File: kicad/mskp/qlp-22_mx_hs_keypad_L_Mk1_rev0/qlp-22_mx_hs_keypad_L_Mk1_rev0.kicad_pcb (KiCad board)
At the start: 2 copper layers, 23 parts, among them J1 Conn_01x12_Socket, SW0 Switch, SW1 Switch, SW10 Switch, SW2 Switch, SW3 Switch, SW4 Switch, SW5 Switch, SW6 Switch, SW7 Switch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

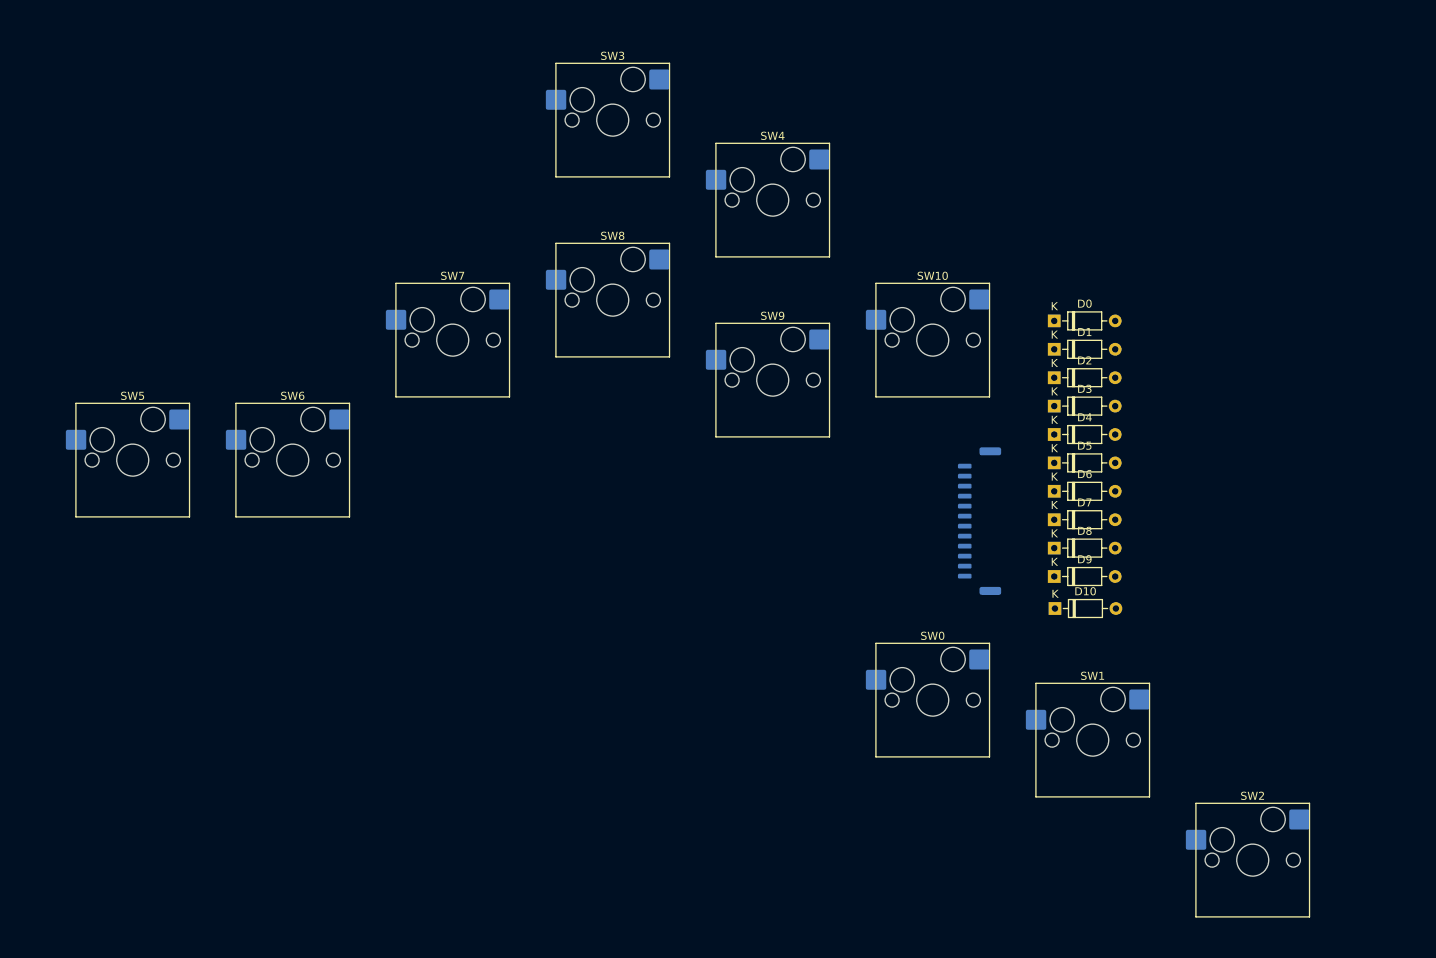
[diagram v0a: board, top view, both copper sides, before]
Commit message: Adds basic layout and edges for qlp-22_mx_hs_keypad_L_Mk1_rev0
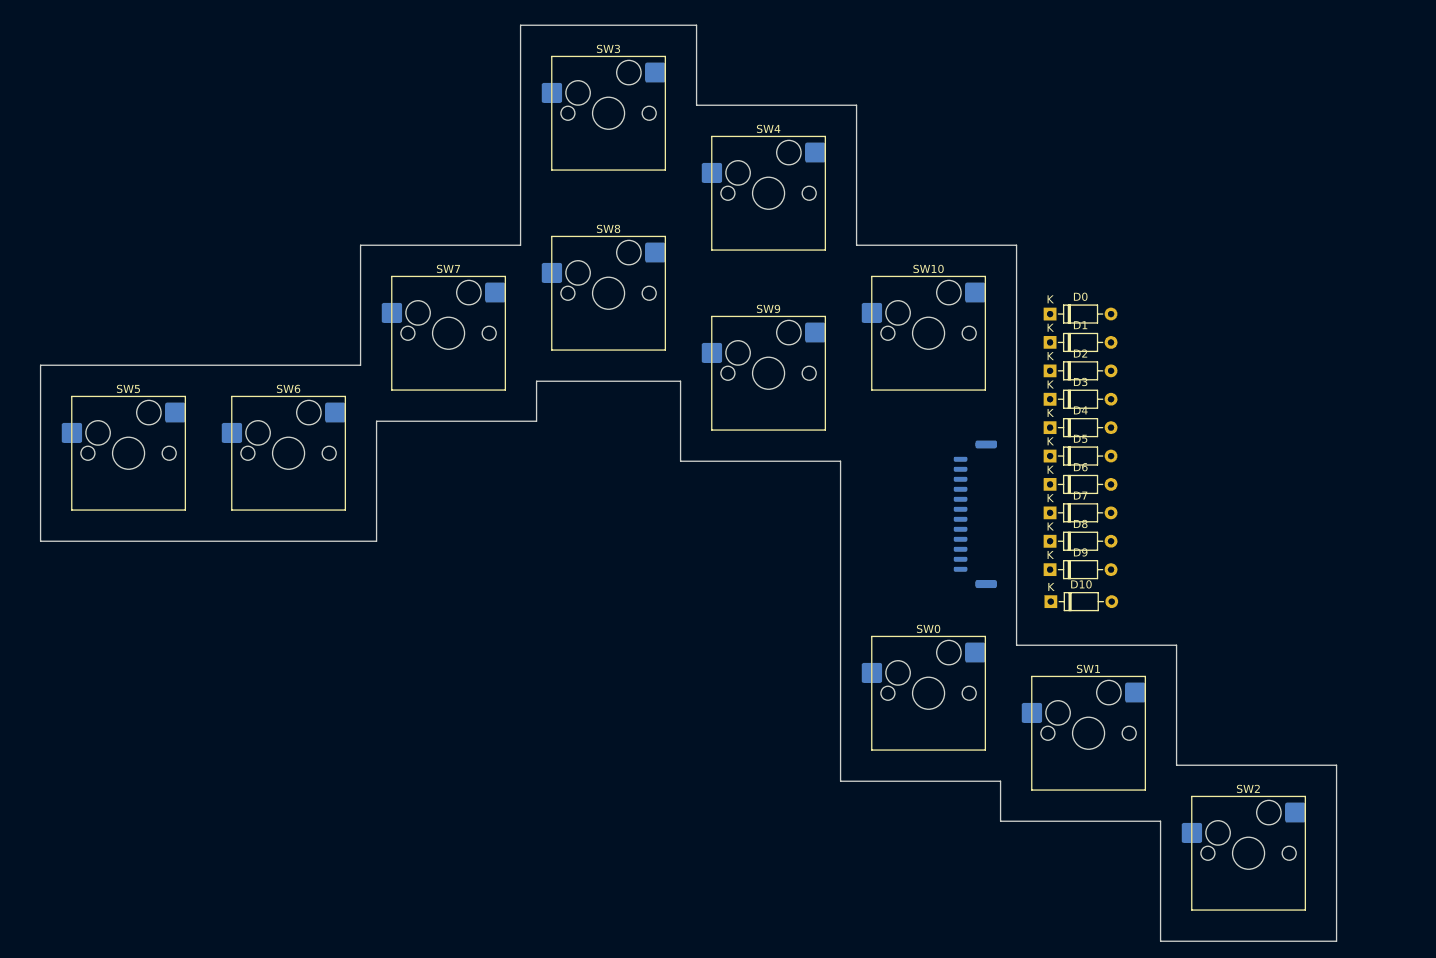
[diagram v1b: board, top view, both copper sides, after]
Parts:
- moved SW5 1.01 mm to (68.5, 79.5)
- moved D0 1.01 mm to (183.7, 62.1)
- moved D10 1.01 mm to (183.8, 98.0)
- moved D2 1.01 mm to (183.7, 69.2)
- moved D3 1.01 mm to (183.7, 72.8)
- moved D4 1.01 mm to (183.7, 76.3)
- moved D7 1.01 mm to (183.7, 87.0)
- moved D8 1.01 mm to (183.7, 90.5)
- moved D9 1.01 mm to (183.7, 94.1)
- moved J1 1.01 mm to (174.3, 87.1)
- moved SW0 1.01 mm to (168.5, 109.5)
- moved SW1 1.01 mm to (188.5, 114.5)
- moved SW10 1.01 mm to (168.5, 64.5)
- moved SW2 1.01 mm to (208.5, 129.5)
- moved SW3 1.01 mm to (128.5, 37.0)
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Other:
- board outline added: 162 x 114.5 mm

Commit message: Add filet, diodes to qlp-22_mx_hs_keypad_L_Mk1_rev0
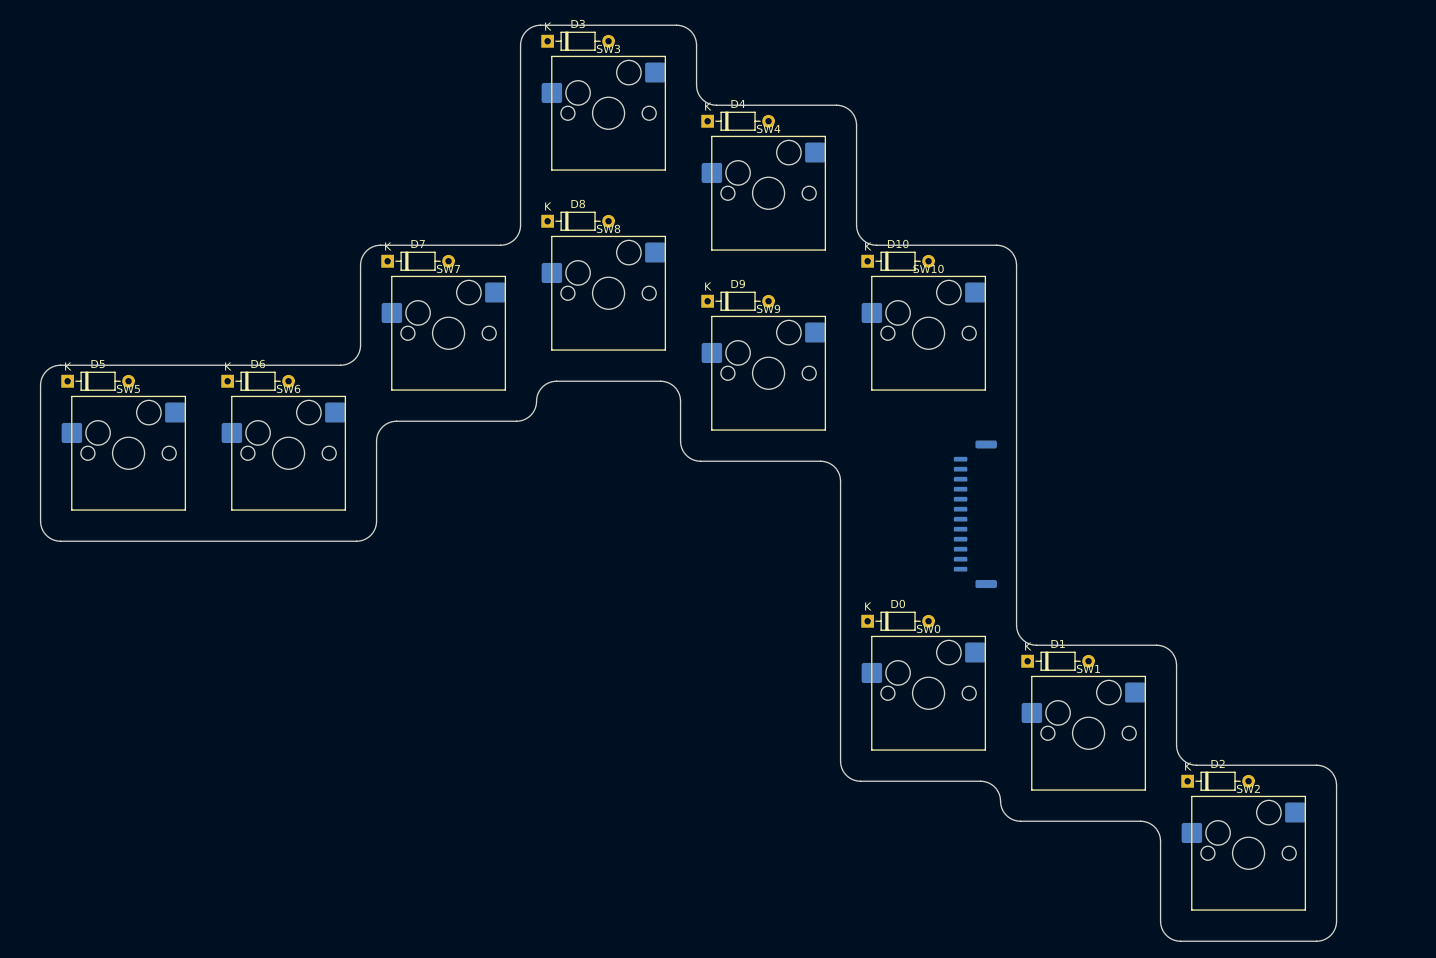
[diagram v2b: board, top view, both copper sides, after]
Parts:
- moved D5 123.2 mm to (60.9, 70.5)
- moved D6 103.6 mm to (80.9, 70.5)
- moved D7 88.6 mm to (100.9, 55.5)
- moved D3 77.1 mm to (120.9, 28.0)
- moved D8 74.5 mm to (120.9, 50.5)
- moved D4 57.4 mm to (140.9, 38.0)
- moved D9 54.4 mm to (140.9, 60.5)
- moved D2 54.1 mm to (200.9, 120.5)
- moved D10 48.3 mm to (160.9, 55.5)
- moved D0 44.7 mm to (160.9, 100.5)
- moved D1 39.9 mm to (180.9, 105.5)
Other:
- outline, holes or cut-outs redrawn

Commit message: Adds wiring for qlp-22_mx_hs_keypad_L_Mk1_rev0
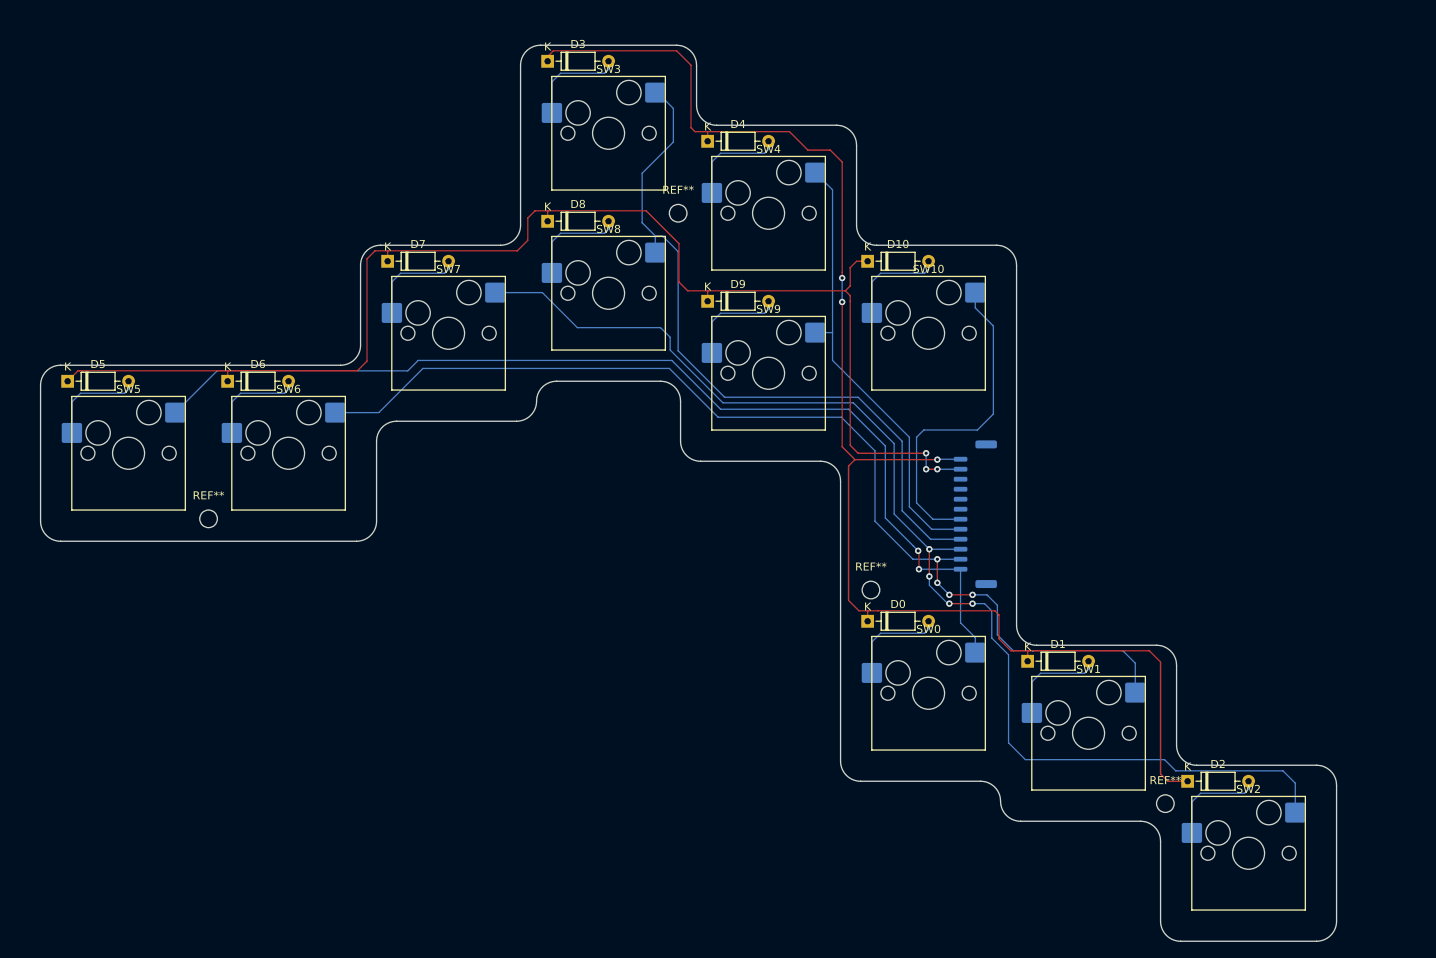
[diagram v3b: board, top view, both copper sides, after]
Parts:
- added REF**: MountingHole_2.2mm_M2_ISO14580, MountingHole:MountingHole_2.2mm_M2_ISO14580, F.Cu at (78.5, 87.7)
- added REF**: MountingHole_2.2mm_M2_ISO14580, MountingHole:MountingHole_2.2mm_M2_ISO14580, F.Cu at (198.1, 123.3)
- added REF**: MountingHole_2.2mm_M2_ISO14580, MountingHole:MountingHole_2.2mm_M2_ISO14580, F.Cu at (137.2, 49.5)
- added REF**: MountingHole_2.2mm_M2_ISO14580, MountingHole:MountingHole_2.2mm_M2_ISO14580, F.Cu at (161.3, 96.6)
- moved D3 2.50 mm to (120.9, 30.5)
- moved SW3 2.50 mm to (128.5, 39.5)
- moved D4 2.50 mm to (140.9, 40.5)
- moved SW4 2.50 mm to (148.5, 49.5)
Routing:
- net Net-(D0-K): track 0.00 -> 182.6 mm, vias 0 -> 3
- net Net-(D10-K): track 0.00 -> 168.8 mm, vias 0 -> 3
- net Net-(J1-Pin_10): track 0.00 -> 150.1 mm, vias 0 -> 4
- net Net-(J1-Pin_11): track 0.00 -> 133.2 mm, vias 0 -> 4
- net Net-(J1-Pin_12): track 0.00 -> 129.4 mm, vias 0 -> 2
- net Net-(J1-Pin_9): track 0.00 -> 89.6 mm
- net Net-(J1-Pin_8): track 0.00 -> 56.4 mm
- net Net-(J1-Pin_7): track 0.00 -> 41.5 mm
- net Net-(D9-A): track 0.00 -> 12.6 mm
- net Net-(D8-A): track 0.00 -> 12.6 mm
- net Net-(D3-A): track 0.00 -> 12.6 mm
- net Net-(D7-A): track 0.00 -> 12.6 mm
- net Net-(D4-A): track 0.00 -> 12.6 mm
- net Net-(D10-A): track 0.00 -> 12.6 mm
- net Net-(D5-A): track 0.00 -> 12.6 mm
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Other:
- board size 162 x 114.5 mm -> 162 x 112 mm

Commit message: Adds logo and OSH symbol to all mskp silkscreens
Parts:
- added G***: LOGO, Desktop:OSH_test, F.Cu at (173.4, 78.8)
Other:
- board text added: "햄"
- board text added: "햄룬드 제조"

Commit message: Partial work on mskp part silkscreens
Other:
- board text added: "03-2024"
- board text added: "HAMLUND MFG."
- board text added: "JLCJLCJLCJLC"
- board text added: "MSKP-QLP-PAD-L-MK.1-REV.0"
- board text added: "Mk I"
- board text added: "QLP MX Keypad L"

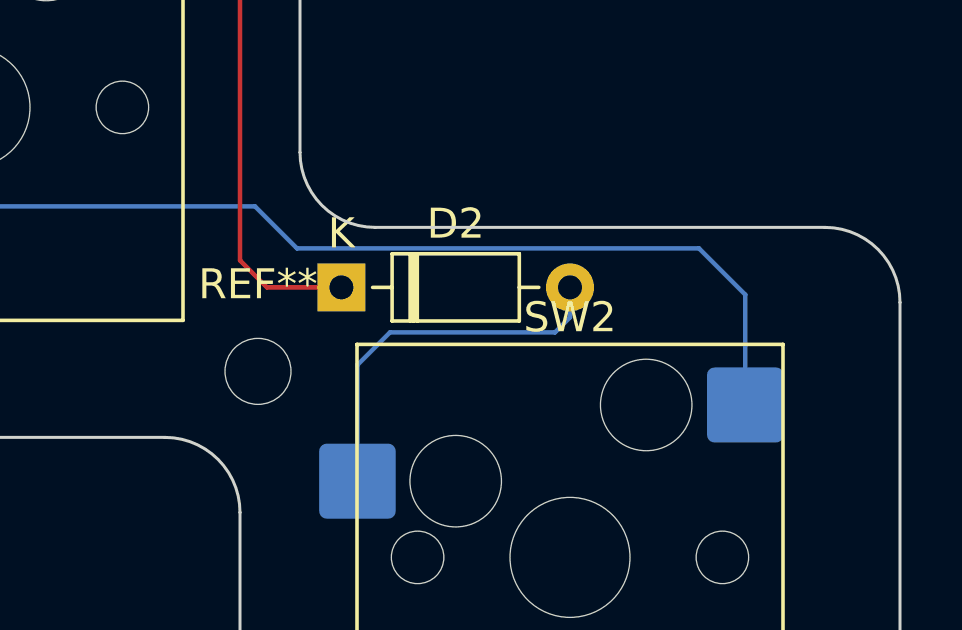
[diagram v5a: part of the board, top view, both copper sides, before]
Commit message: Cleans up unneeded files and adds more silkscreen tidy
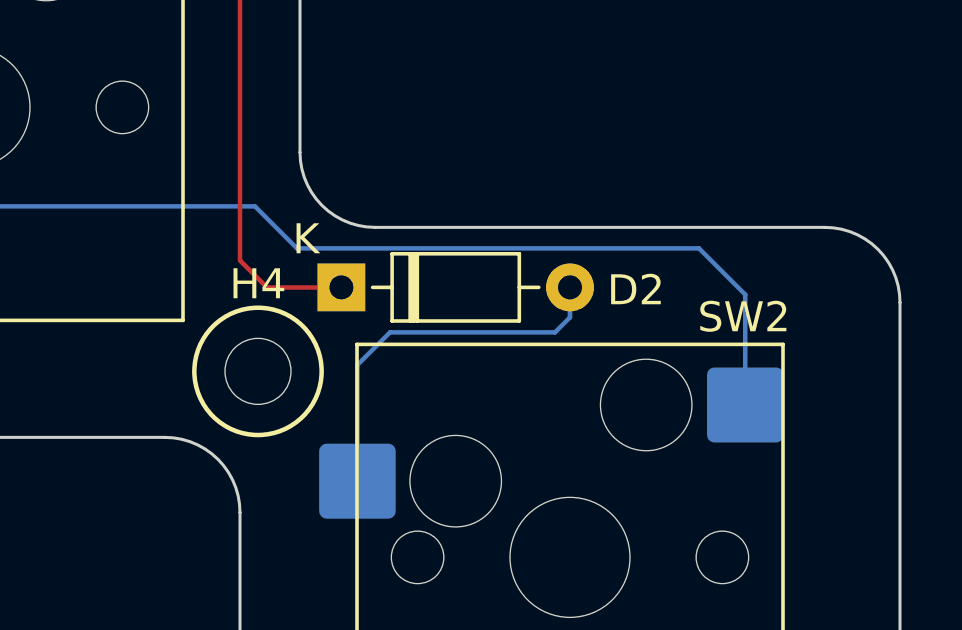
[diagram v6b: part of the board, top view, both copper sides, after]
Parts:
- renumbered REF** to H4
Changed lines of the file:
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@@
     (tags "mounting hole 2.2mm no annular m2 iso14580")
     (attr exclude_from_pos_files exclude_from_bom)
-    (fp_text reference "REF**" (at 0 -2.9) (layer "F.SilkS")
+    (fp_text reference "H4" (at 0 -2.9) (layer "F.SilkS")
         (effects (font (size 1 1) (thickness 0.15)))
     )
@@
     (property "ki_keywords" "diode")
     (attr through_hole)
-    (fp_text reference "D2" (at 3.81 -2.12) (layer "F.SilkS")
+    (fp_text reference "D2" (at 9.820002 0.1) (layer "F.SilkS")
         (effects (font (size 1 1) (thickness 0.15)))
     )
@@
         (effects (font (size 1 1) (thickness 0.15)))
     )
-    (fp_text user "K" (at 0 -1.8) (layer "F.SilkS")
+    (fp_text user "K" (at -1.179998 -1.6) (layer "F.SilkS")
         (effects (font (size 1 1) (thickness 0.15)))
     )
@@
     (property "ki_keywords" "switch normally-open pushbutton push-button")
     (attr smd)
-    (fp_text reference "SW2" (at 0 -8) (layer "F.SilkS")
+    (fp_text reference "SW2" (at 5.800002 -8) (layer "F.SilkS")
         (effects (font (size 1 1) (thickness 0.15)))
     )
@@
     )
   )
+  (gr_circle (center 198.1 123.3) (end 199.6 124.8)
+    (stroke (width 0.15) (type default)) (fill none) (layer "F.SilkS"))
   (gr_line (start 159.1 87.1) (end 175.1 87.1)
     (stroke (width 0.15) (type default)) (layer "F.SilkS"))
